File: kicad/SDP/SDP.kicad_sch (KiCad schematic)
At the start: 83 parts, among them J1 GPIO, J2 SPI, J24 POWER, J25 Conn_01x04, J26 Conn_01x02, J3 UART, J4 I2C, J5 Conn_01x04, J6 Conn_01x04, J7 RJ25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

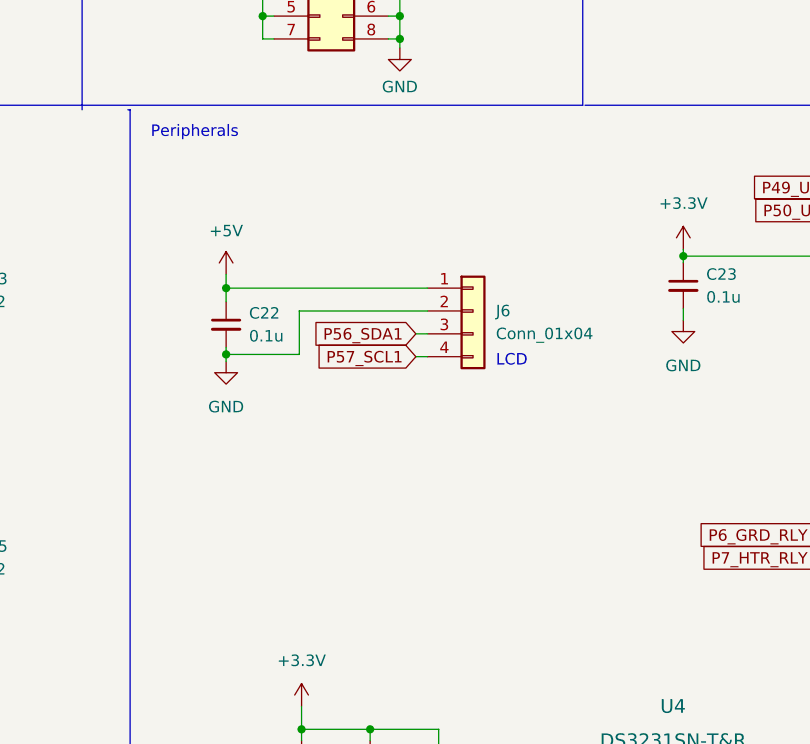
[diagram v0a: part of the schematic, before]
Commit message: Separated control and motor boards
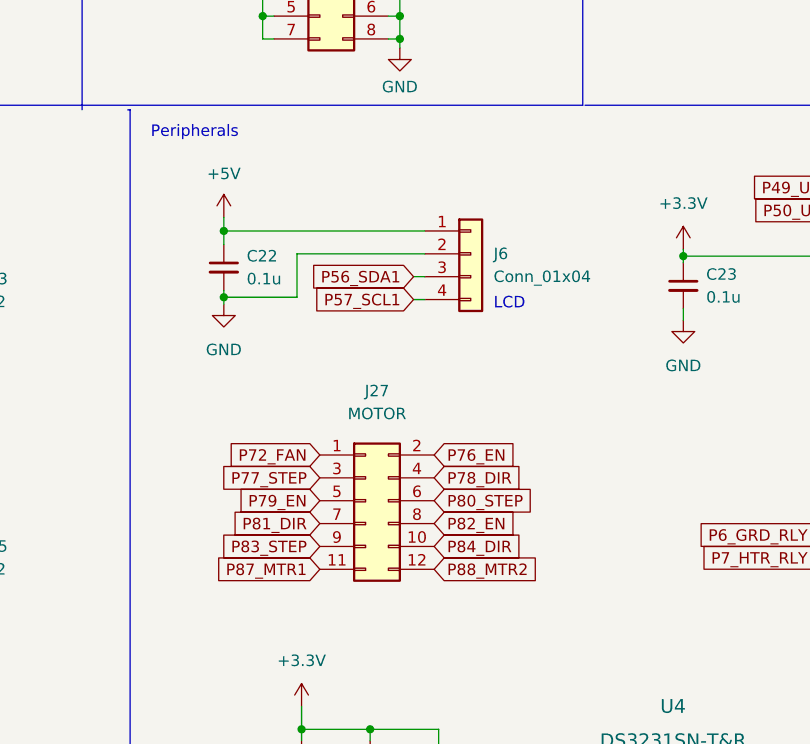
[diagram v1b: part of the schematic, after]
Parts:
- added J27: MOTOR, Connector_PinSocket_2.54mm:PinSocket_2x04_P2.54mm_Vertical, symbol Connector_Generic:Conn_02x06_Odd_Even
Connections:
- net P72_FAN: now also J27.1 (Pin_1)
- net P76_EN: now also J27.2 (Pin_2)
- net P77_STEP: now also J27.3 (Pin_3)
- net P78_DIR: now also J27.4 (Pin_4)
- net P79_EN: now also J27.5 (Pin_5)
- net P80_STEP: now also J27.6 (Pin_6)
- net P81_DIR: now also J27.7 (Pin_7)
- net P82_EN: now also J27.8 (Pin_8)
- net P83_STEP: now also J27.9 (Pin_9)
- net P84_DIR: now also J27.10 (Pin_10)
- net P87_MTR1: now also J27.11 (Pin_11)
- net P88_MTR2: now also J27.12 (Pin_12)
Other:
- moved on the sheet: C22, J6

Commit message: PCB layout of main controller board
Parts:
- removed J27: MOTOR, Connector_PinSocket_2.54mm:PinSocket_2x04_P2.54mm_Vertical, symbol Connector_Generic:Conn_02x06_Odd_Even
- added H1, H2, H3, H4: MountingHole_Pad, MountingHole:MountingHole_3.2mm_M3_Pad, symbol Mechanical:MountingHole_Pad
- added J27: MOTOR, Connector_PinSocket_2.54mm:PinSocket_2x08_P2.54mm_Vertical, symbol Connector_Generic:Conn_02x08_Odd_Even
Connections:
- net +12V: now also J27.15 (Pin_15)
- net +3V3: now also J27.1 (Pin_1), J27.2 (Pin_2)
- net GND: now also H1.1, H2.1, H3.1, H4.1, J27.16 (Pin_16)
- net P56_SDA1: now also J4.4 (Pin_4); no longer J4.1 (Pin_1)
- net P57_SCL1: now also J4.2 (Pin_2); no longer J4.3 (Pin_3)
- net P58_SCL2: now also J4.3 (Pin_3); no longer J4.4 (Pin_4)
- net P59_SDA2: now also J4.1 (Pin_1); no longer J4.2 (Pin_2)
- net P72_FAN: now also J27.3 (Pin_3)
- net P76_EN: now also J27.4 (Pin_4)
- net P77_STEP: now also J27.5 (Pin_5)
- net P78_DIR: now also J27.6 (Pin_6)
- net P79_EN: now also J27.7 (Pin_7)
- net P80_STEP: now also J27.8 (Pin_8)
- net P81_DIR: now also J27.9 (Pin_9)
- net P82_EN: now also J27.10 (Pin_10)
- net P83_STEP: now also J27.11 (Pin_11)
- net P84_DIR: now also J27.12 (Pin_12)
- net P87_MTR1: now also J27.13 (Pin_13)
- net P88_MTR2: now also J27.14 (Pin_14)
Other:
- removed sheet StepperMotors
- removed sheet WaterSubsystem
- moved on the sheet: TP1, TP2, TP3, TP4

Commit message: Controller PCB layout
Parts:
- removed J2: SPI, Connector_PinSocket_2.54mm:PinSocket_2x04_P2.54mm_Vertical, symbol Connector_Generic:Conn_02x04_Odd_Even
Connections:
- net P18_RE8: now also J1.4 (Pin_4); no longer J1.2 (Pin_2)
- net P19_RE9: now also J1.3 (Pin_3); no longer J1.1 (Pin_1)
- net P1_RG15: now also J1.14 (Pin_14); no longer J1.5 (Pin_5)
- net P20_RB5: now also J1.2 (Pin_2); no longer J1.4 (Pin_4)
- net P21_RB4: now also J1.1 (Pin_1); no longer J1.3 (Pin_3)
- net P3_RE5: now also J1.13 (Pin_13); no longer J1.6 (Pin_6)
- net P49_U2RX: now also J3.4 (Pin_4); no longer J3.3 (Pin_3)
- net P4_RE6: now also J1.12 (Pin_12); no longer J1.7 (Pin_7)
- net P50_U2TX: now also J3.2 (Pin_2); no longer J3.1 (Pin_1)
- net P51_U1TX: now also J3.1 (Pin_1); no longer J3.2 (Pin_2)
- net P52_U1RX: now also J3.3 (Pin_3); no longer J3.4 (Pin_4)
- net P58_SCL2: now also J4.1 (Pin_1); no longer J4.3 (Pin_3)
- net P59_SDA2: now also J4.3 (Pin_3); no longer J4.1 (Pin_1)
- net P5_RE7: now also J1.11 (Pin_11); no longer J1.8 (Pin_8)
- net P66_RA14: now also J1.5 (Pin_5); no longer J1.9 (Pin_9)
- net P67_RA15: now also J1.6 (Pin_6); no longer J1.11 (Pin_11)
- net P68_RD8: now also J1.7 (Pin_7); no longer J1.10 (Pin_10)
- net P69_RD9: now also J1.8 (Pin_8); no longer J1.12 (Pin_12)
- net P70_RD10: now also J1.9 (Pin_9); no longer J1.13 (Pin_13)
- net P71_RD11: now also J1.10 (Pin_10); no longer J1.14 (Pin_14)
- net P89_RG1: now also J1.17 (Pin_17); no longer J1.15 (Pin_15)
- net P90_RG0: now also J1.18 (Pin_18); no longer J1.16 (Pin_16)
- net P93_RE0: now also J1.15 (Pin_15); no longer J1.17 (Pin_17)
- net P94_RE1: now also J1.16 (Pin_16); no longer J1.18 (Pin_18)
- net P33_TOF2_CE renamed P33_TOF1_GPIO1
- net P34_TOF3_CE renamed P34_TOF2_CE
- net P35_TOF4_CE renamed P35_TOF2_GPIO1
- net P41_TOF1_GPIO1 renamed P41_TOF3_CE
- net P42_TOF2_GPIO1 renamed P42_TOF3_GPIO1
- net P43_TOF3_GPIO1 renamed P43_TOF4_CE
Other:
- moved on the sheet: J1, J24, J3, J4

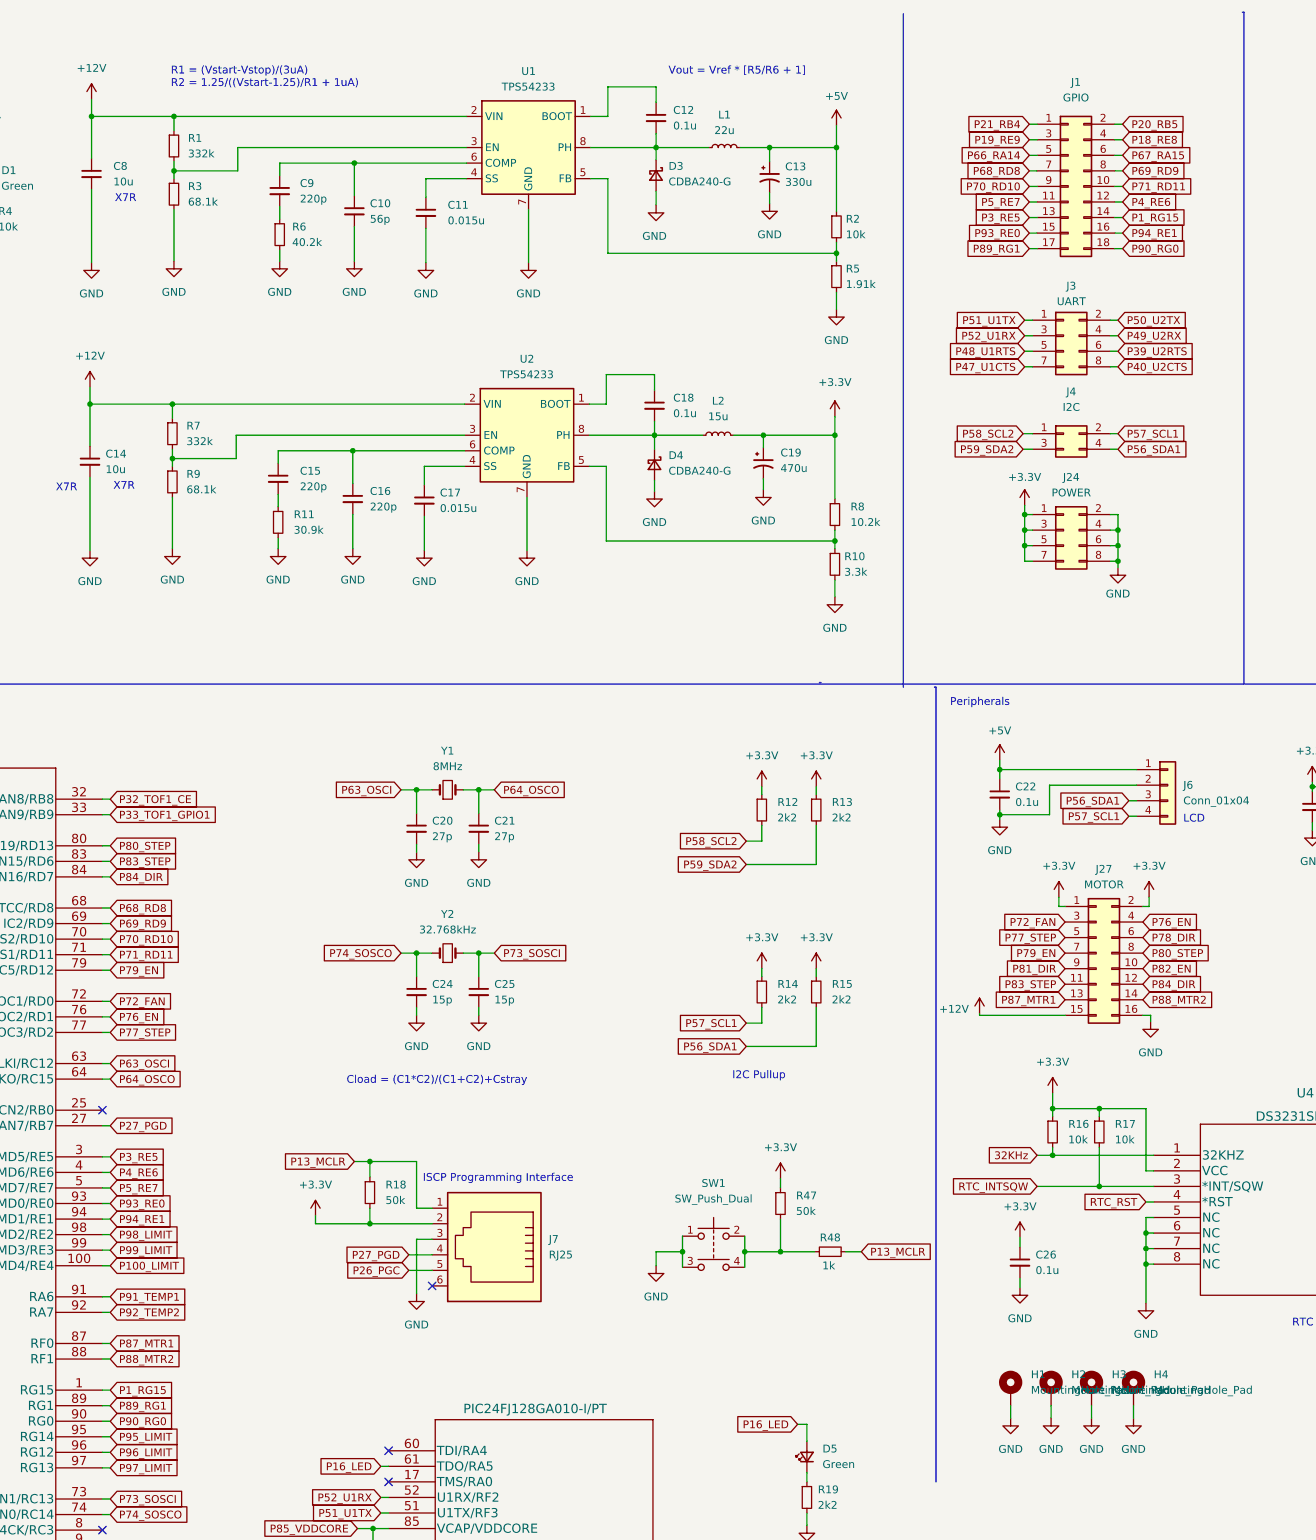
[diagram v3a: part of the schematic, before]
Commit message: Added proximity sensor headers
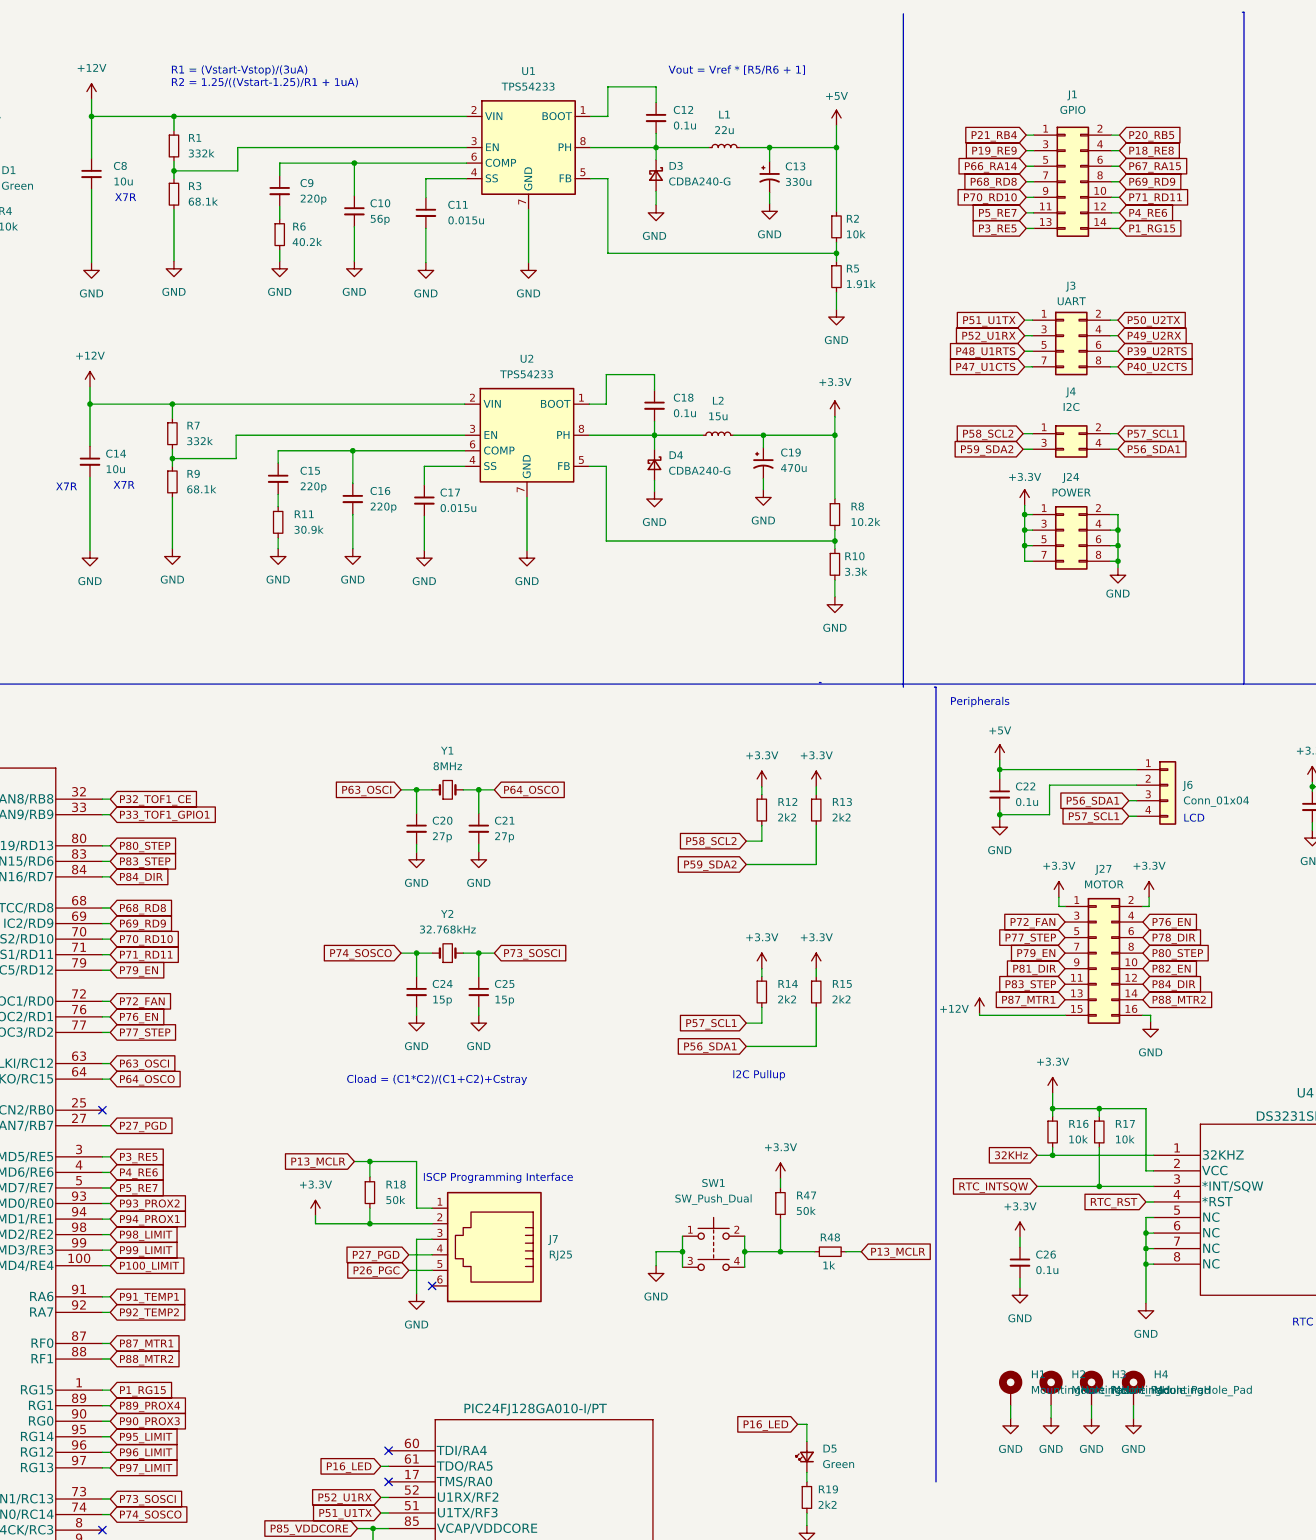
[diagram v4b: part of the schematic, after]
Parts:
- removed J1: GPIO, Connector_PinSocket_2.54mm:PinSocket_2x09_P2.54mm_Vertical, symbol Connector_Generic:Conn_02x09_Odd_Even
- added J1: GPIO, Connector_PinSocket_2.54mm:PinSocket_2x07_P2.54mm_Vertical, symbol Connector_Generic:Conn_02x07_Odd_Even
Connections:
- net P18_RE8: now also J1.4 (Pin_4)
- net P19_RE9: now also J1.3 (Pin_3)
- net P1_RG15: now also J1.14 (Pin_14)
- net P20_RB5: now also J1.2 (Pin_2)
- net P21_RB4: now also J1.1 (Pin_1)
- net P3_RE5: now also J1.13 (Pin_13)
- net P4_RE6: now also J1.12 (Pin_12)
- net P5_RE7: now also J1.11 (Pin_11)
- net P66_RA14: now also J1.5 (Pin_5)
- net P67_RA15: now also J1.6 (Pin_6)
- net P68_RD8: now also J1.7 (Pin_7)
- net P69_RD9: now also J1.8 (Pin_8)
- net P70_RD10: now also J1.9 (Pin_9)
- net P71_RD11: now also J1.10 (Pin_10)
- net P89_RG1 renamed P89_PROX4
- net P90_RG0 renamed P90_PROX3
- net P93_RE0 renamed P93_PROX2
- net P94_RE1 renamed P94_PROX1

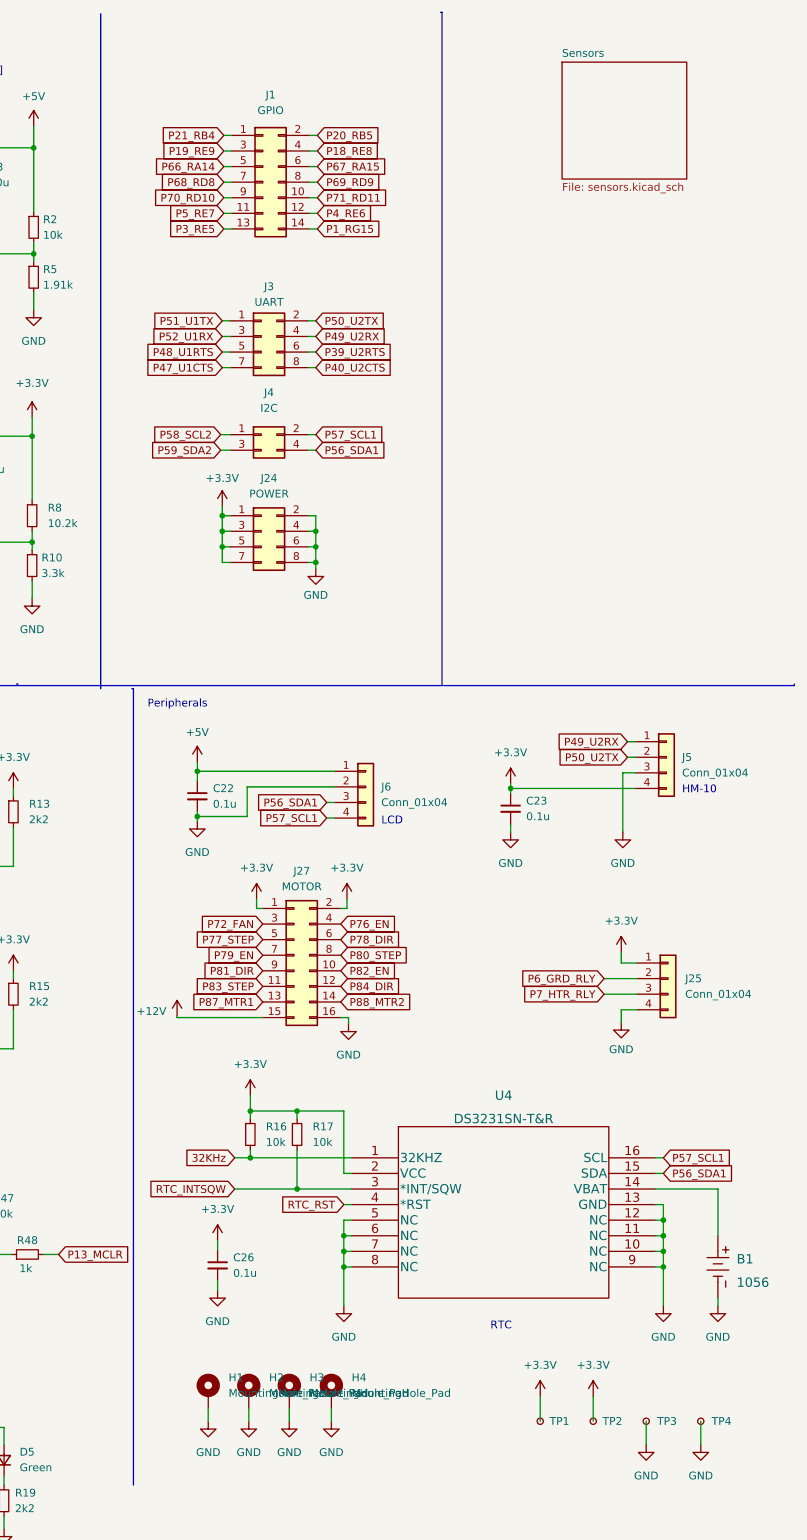
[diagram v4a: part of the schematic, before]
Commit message: Motor PCB layout
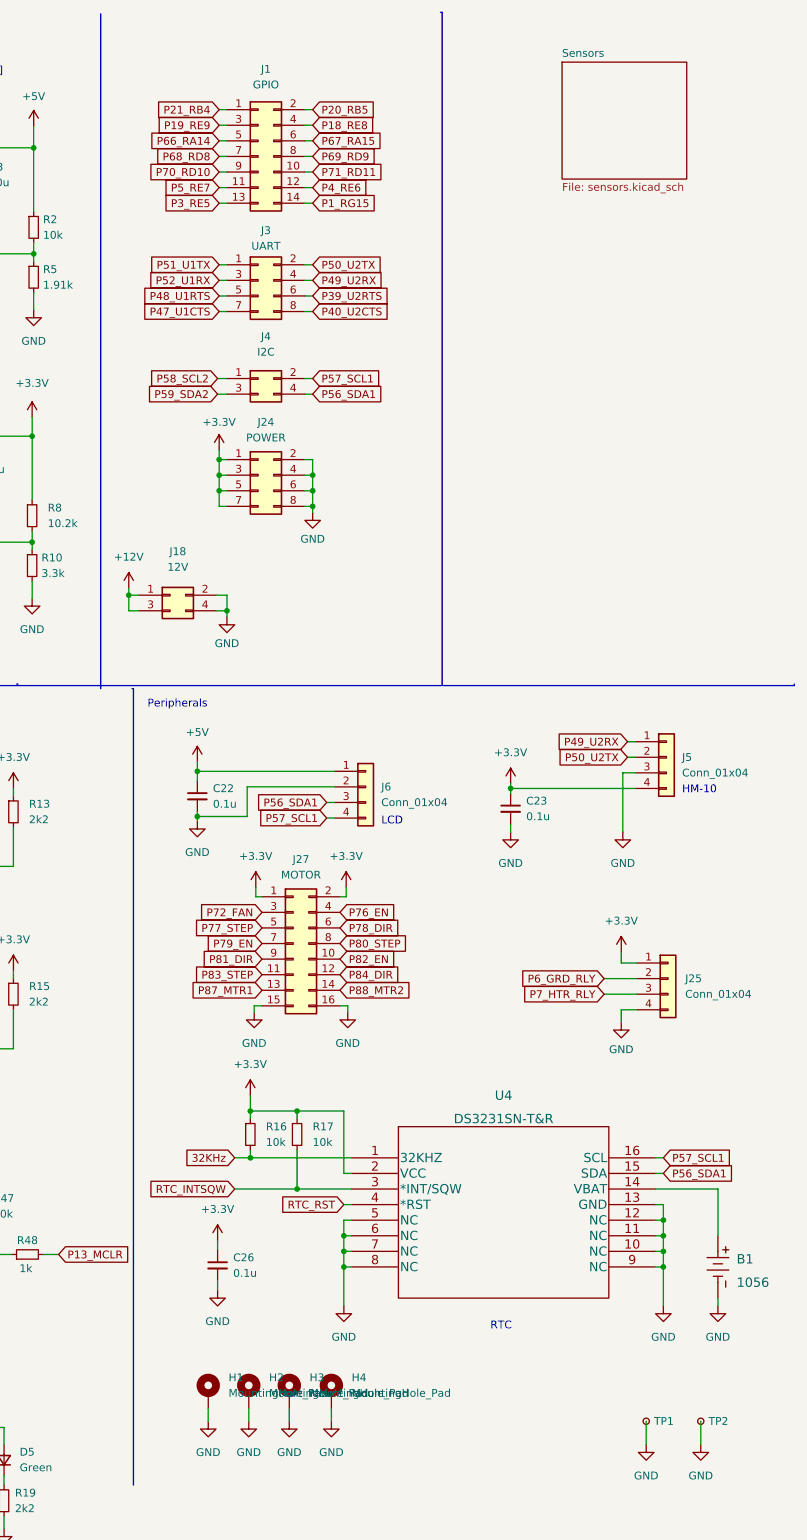
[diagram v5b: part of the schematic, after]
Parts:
- removed TP1, TP2: TestPoint_Small, TestPoint:TestPoint_Pad_D2.0mm, symbol Connector:TestPoint_Small
- added J18: 12V, Connector_PinSocket_2.54mm:PinSocket_2x02_P2.54mm_Vertical, symbol Connector_Generic:Conn_02x02_Odd_Even
- TP1: renamed from TP3; footprint TestPoint:TestPoint_Pad_D2.0mm -> TestPoint:TestPoint_Keystone_5005-5009_Compact
- TP2: renamed from TP4; footprint TestPoint:TestPoint_Pad_D2.0mm -> TestPoint:TestPoint_Keystone_5005-5009_Compact
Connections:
- net +12V: now also J18.1 (Pin_1), J18.3 (Pin_3); no longer J27.15 (Pin_15)
- net GND: now also J27.15 (Pin_15), J18.2 (Pin_2), J18.4 (Pin_4)
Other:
- moved on the sheet: J1, J24, J27, J3, J4
